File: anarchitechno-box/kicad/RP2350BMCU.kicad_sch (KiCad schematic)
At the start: 51 parts, among them J1 C2988369, J10 Conn_01x04, J2 Conn_01x03_Socket, J8 Conn_01x04, Q1 12mhz, SW1 C318884, SW2 RotaryEncoder_Switch_MP, U4 <value>, U6 TLV74311PDBVR, U7 C85364

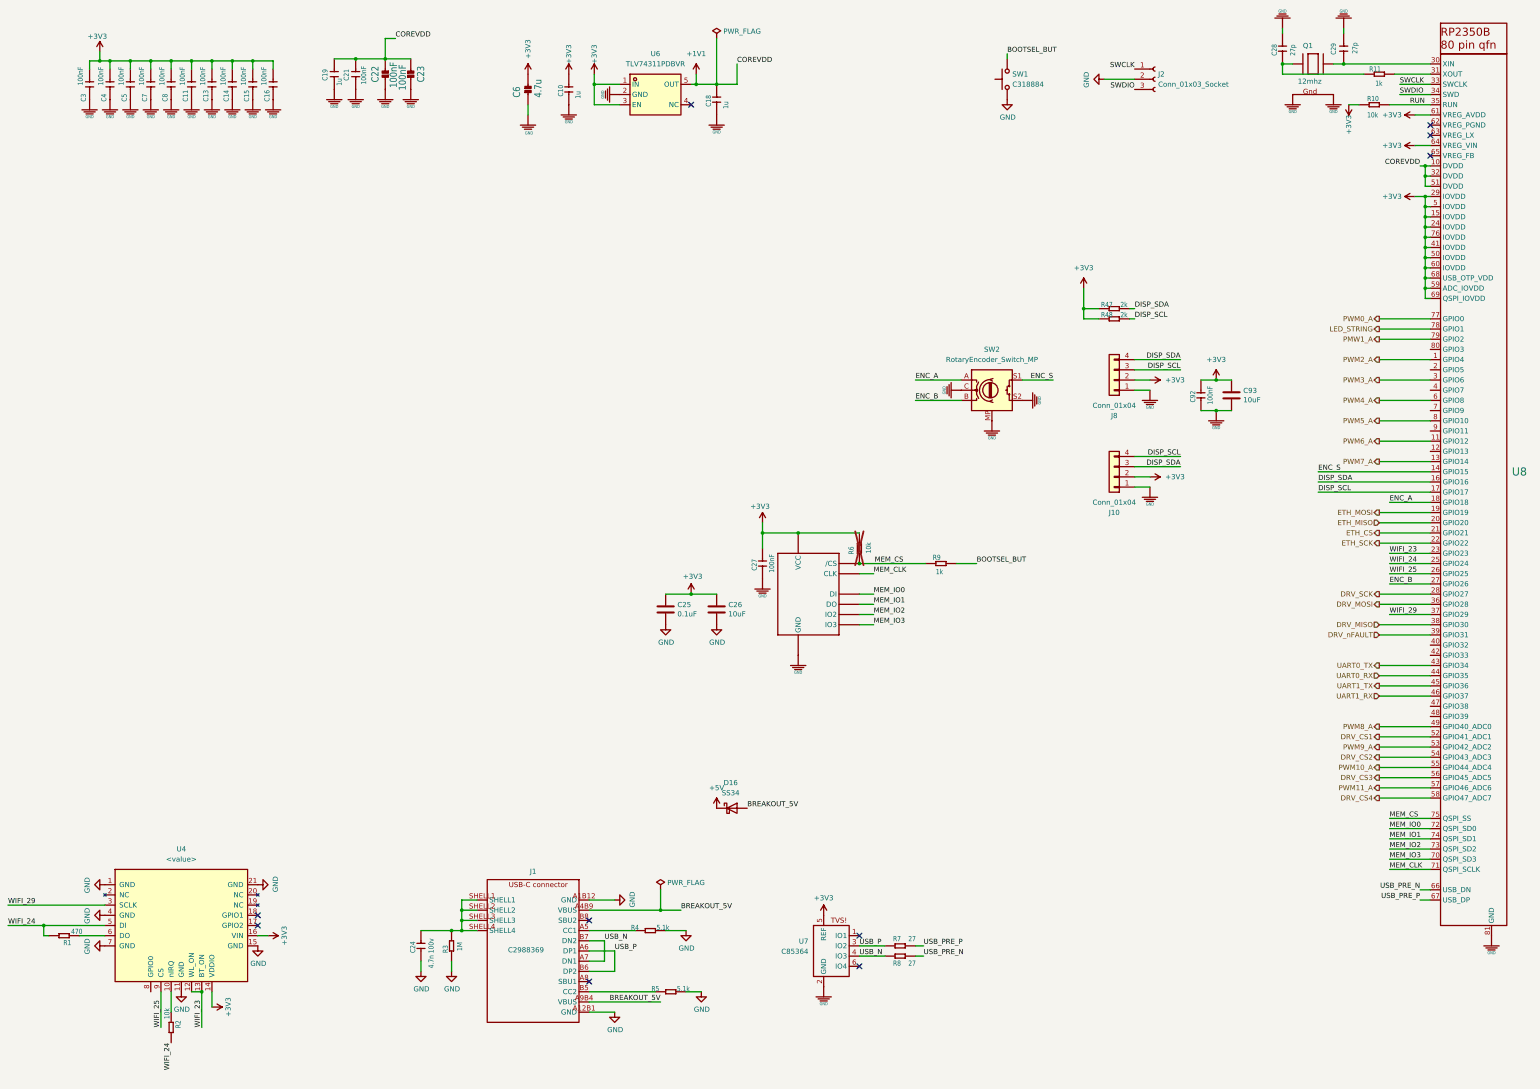
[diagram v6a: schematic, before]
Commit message: Schematic & PCB changes: - Cleaned up unnecessary electrolytic input capacitor flyback - Removed dual diode rectification on 5V, increased output capacitors - Feedback resistors DC/DCs set, enlarged for JLC basic parts - Sweep through schematic to consolidate caps to JLC basic parts (see list schematic front page) - Midi OUTPUT added (please check schematic) - Wiznet W5500 schematic reworked to RJ45 reference schematic: https://docs.wiznet.io/assets/files/w5500_sch_v110_use_mag_-dfff8bbb103d13be4f25cd2b2f8b950d.pdf - Replaced ethernet jack to HR911105A - Crystals chosen for W5500 and RP2350B (according to reference), 15pF load caps. - RS485 driver changed to SP3485EN for 3.3V operation - Replaced RS485 bus connectors with 2x RJ45s for passthrough - Groove connector replaced with JST XH 2mm - Added LCSC part numbers for various components in the schematic
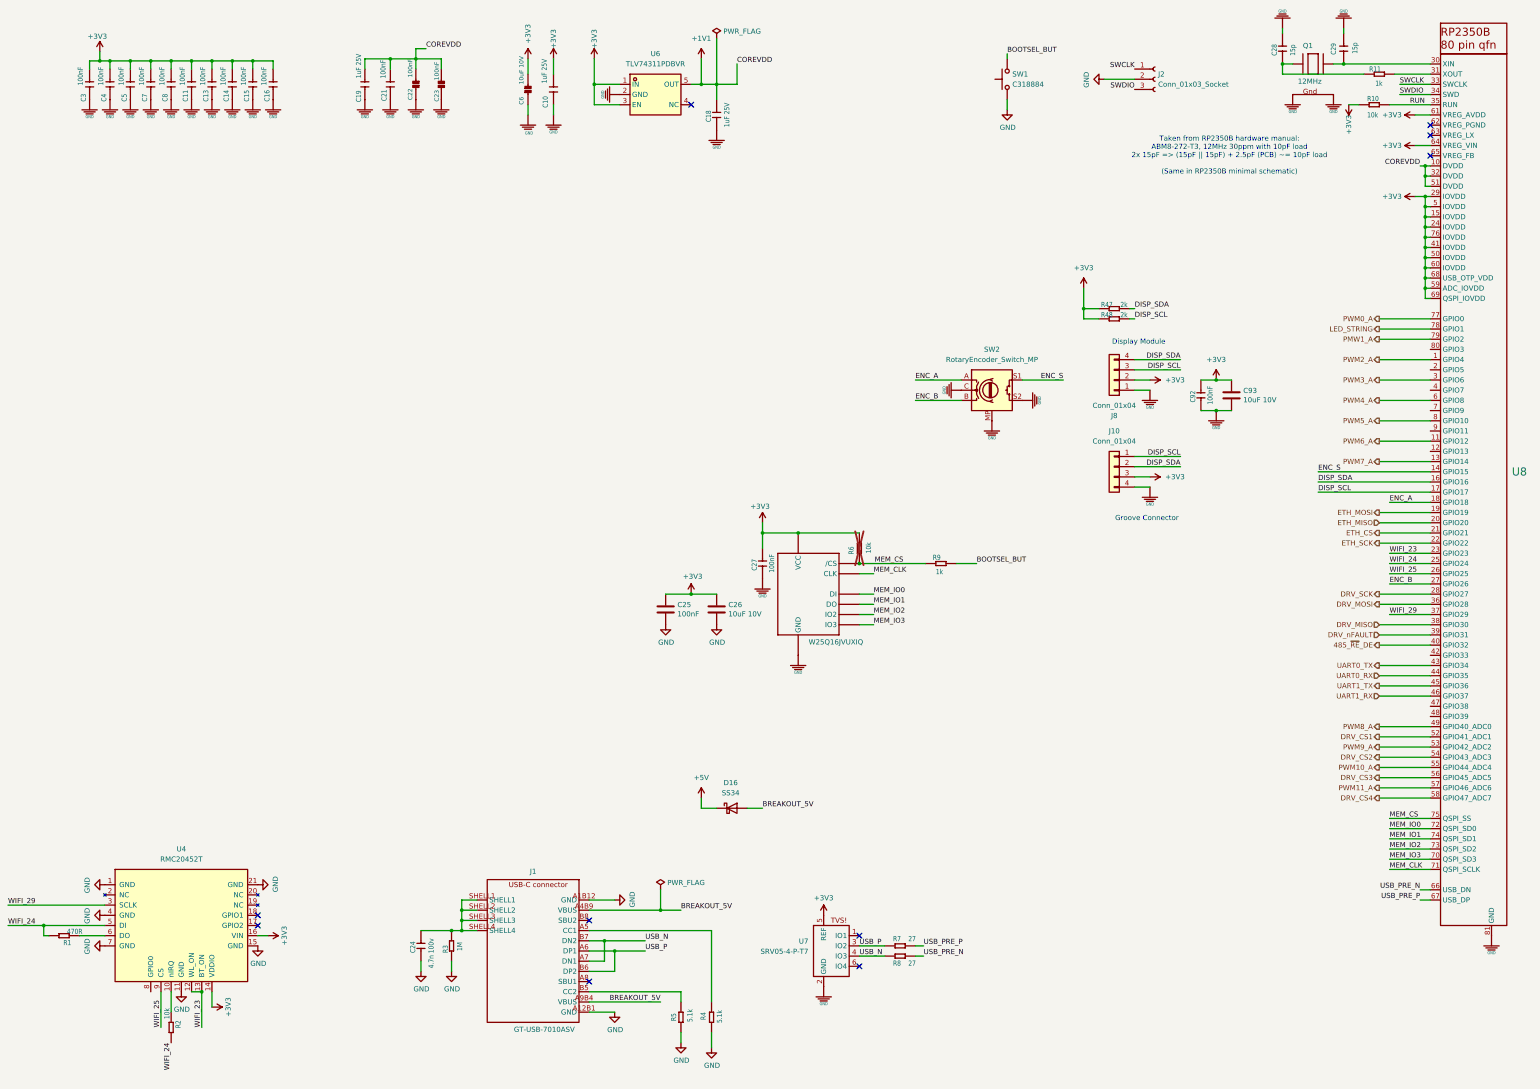
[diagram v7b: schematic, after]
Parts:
- C10, C18: value 1u -> 1uF 25V; LCSC Part (none) -> C52923
- C19: value 1u -> 1uF 25V; LSCS Part (none) -> C52923
- C24: LCSC Part (none) -> C577156
- C25: value 0.1uF -> 100nF; Digi-Key_PN 311-1344-1-ND -> (none)
- C26, C93: value 10uF -> 10uF 10V; Digi-Key_PN 311-1344-1-ND -> (none); LCSC Part (none) -> C19702
- C28, C29: value 27p -> 15p; LCSC Part (none) -> C1548
- C6: value 4.7u -> 10uF 10V; footprint Capacitor_SMD:C_0402_1005Metric -> Capacitor_SMD:C_0603_1608Metric; LCSC Part (none) -> C19702
- J1: value C2988369 -> GT-USB-7010ASV; LCSC Part (none) -> C2988369
- J10: footprint Connector_PinHeader_2.54mm:PinHeader_1x04_P2.54mm_Vertical -> Connectors:Grove_1x04
- Q1: value 12mhz -> 12MHz; LCSC Part (none) -> C20625731
- R1: value 470 -> 470R; footprint Resistor_SMD:R_0603_1608Metric -> Resistor_SMD:R_0402_1005Metric
- R2: footprint Resistor_SMD:R_0603_1608Metric -> Resistor_SMD:R_0402_1005Metric
- R3: LCSC Part (none) -> C22935
- R4, R5: LCSC Part (none) -> C23186
- SW1: LCSC Part (none) -> C318884
- U$1: value C2843335 W25Q16JVUXIQ -> W25Q16JVUXIQ; LCSC Part (none) -> C2843335
- U4: value <value> -> RMC20452T; LCSC Part (none) -> C49451547
- U7: value C85364 -> SRV05-4-P-T7; LCSC Part (none) -> C85364
- U8: LCSC Part (none) -> C42415655
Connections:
- net +3V3: now also J10.3 (Pin_3); no longer J10.2 (Pin_2)
- net DISP_SCL: now also J10.1 (Pin_1); no longer J10.4 (Pin_4)
- net DISP_SDA: now also J10.2 (Pin_2); no longer J10.3 (Pin_3)
- net GND: now also J10.4 (Pin_4); no longer J10.1 (Pin_1)
- net 485_~{RE}_DE: now reaches U8.40 (GPIO32)
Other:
- note added: "Display Module"
- note added: "Groove Connector"
- note added: "Taken from RP2350B hardware manual: ABM8-272-T3, 12MHz 30ppm with 10pF load 2x 15pF => (15pF || 15pF) + 2.5pF (PCB) ~= 10pF load (Same in RP2350B minimal schematic)"
- moved on the sheet: C10, C18, C19, C21, C22, C23, J10, R4, R5

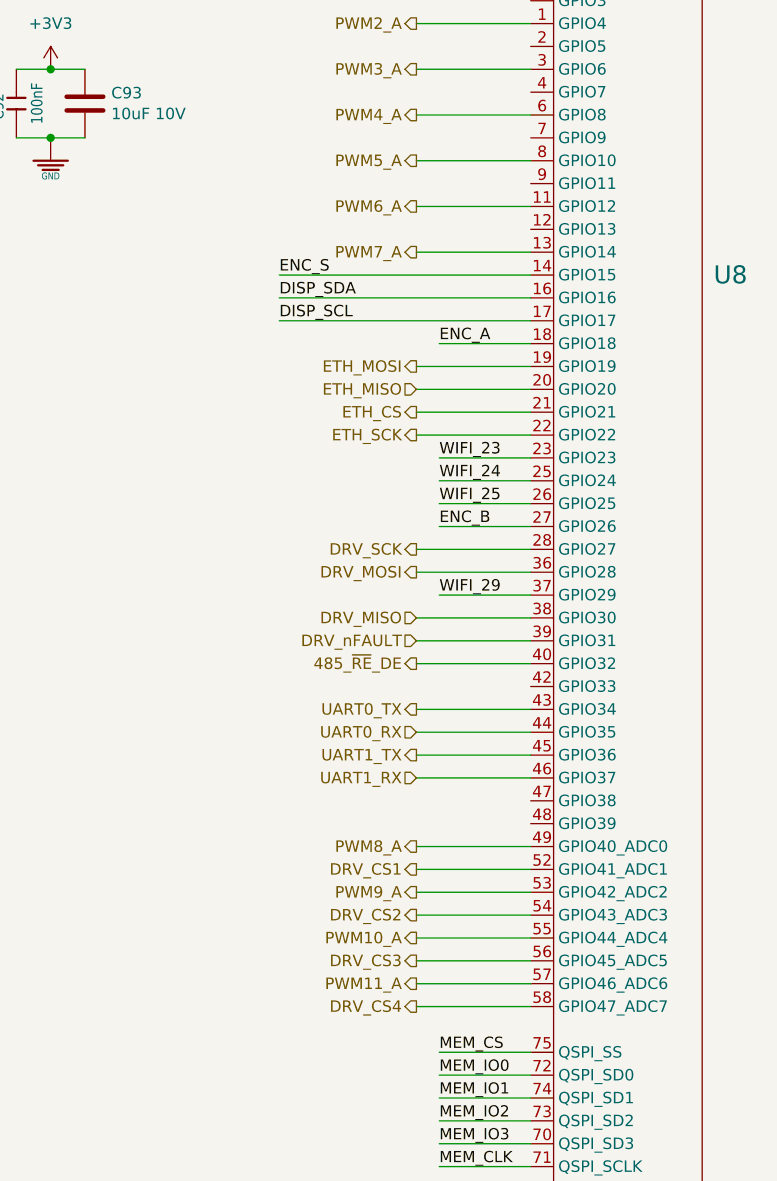
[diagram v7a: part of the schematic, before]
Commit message: - Thermische berekening DRV8245 vs losse transistors - DRV8245 package gecorrigeerd naar TSSOP-28 - Layout aangepast om grotere package te passen - 1x GND output per kanaal - Waarschijnlijk geen 140mm fan nodig => print weer gekropmen - RS485 power line gefixed (3.3V vs 3V3P) - Kleine BOM en I/O wijzigingen tbv layout
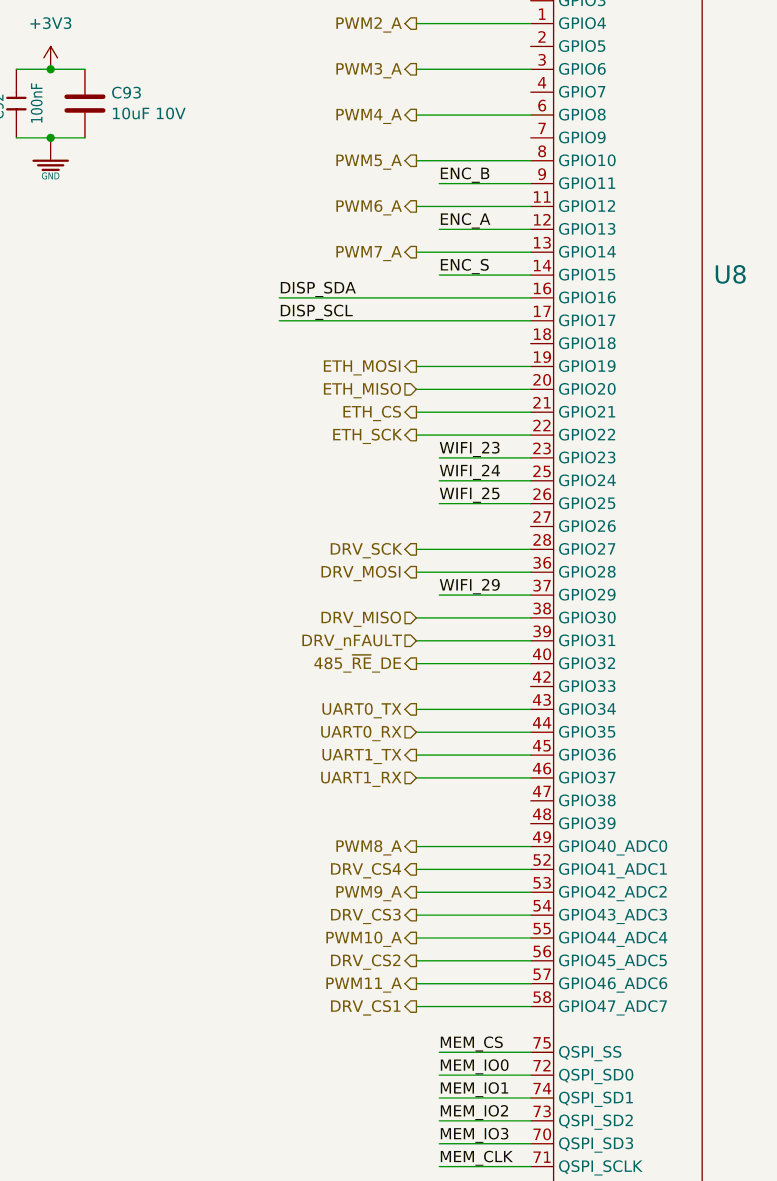
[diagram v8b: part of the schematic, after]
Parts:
- R7, R8: footprint Resistor_SMD:R_0603_1608Metric -> Resistor_SMD:R_0402_1005Metric; LCSC Part (none) -> C138021
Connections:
- net DRV_CS1: now also U8.58 (GPIO47_ADC7); no longer U8.52 (GPIO41_ADC1)
- net DRV_CS2: now also U8.56 (GPIO45_ADC5); no longer U8.54 (GPIO43_ADC3)
- net DRV_CS3: now also U8.54 (GPIO43_ADC3); no longer U8.56 (GPIO45_ADC5)
- net DRV_CS4: now also U8.52 (GPIO41_ADC1); no longer U8.58 (GPIO47_ADC7)
- net ENC_A: now also U8.12 (GPIO13); no longer U8.18 (GPIO18)
- net ENC_B: now also U8.9 (GPIO11); no longer U8.27 (GPIO26)
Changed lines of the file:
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@@
 	(wire
 		(pts
-			(xy 351.79 130.81) (xy 379.73 130.81)
-		)
-		(stroke
-			(width 0)
-			(type default)
-		)
-	)
-	(wire
-		(pts
 			(xy 243.84 248.92) (xy 237.49 248.92)
 		)
@@
 	(wire
 		(pts
+			(xy 367.03 207.01) (xy 379.73 207.01)
+		)
+		(stroke
+			(width 0)
+			(type default)
+		)
+	)
+	(wire
+		(pts
 			(xy 317.5 105.41) (xy 306.07 105.41)
 		)
@@
 	(wire
 		(pts
+			(xy 367.03 201.93) (xy 379.73 201.93)
+		)
+		(stroke
+			(width 0)
+			(type default)
+		)
+	)
+	(wire
+		(pts
 			(xy 361.95 39.37) (xy 359.41 39.37)
 		)
@@
 	(wire
 		(pts
-			(xy 367.03 196.85) (xy 379.73 196.85)
+			(xy 237.49 166.37) (xy 241.046 166.37)
 		)
 		(stroke
@@
 	(wire
 		(pts
-			(xy 237.49 166.37) (xy 241.046 166.37)
+			(xy 377.19 234.95) (xy 379.73 234.95)
 		)
 		(stroke
@@
 	(wire
 		(pts
-			(xy 377.19 234.95) (xy 379.73 234.95)
+			(xy 367.03 196.85) (xy 379.73 196.85)
 		)
 		(stroke
@@
 	(wire
 		(pts
-			(xy 369.57 158.75) (xy 379.73 158.75)
-		)
-		(stroke
-			(width 0)
-			(type default)
-		)
-	)
-	(wire
-		(pts
 			(xy 48.26 26.162) (xy 48.26 28.448)
 		)
@@
 	(wire
 		(pts
+			(xy 367.03 212.09) (xy 379.73 212.09)
+		)
+		(stroke
+			(width 0)
+			(type default)
+		)
+	)
+	(wire
+		(pts
 			(xy 378.46 54.61) (xy 379.73 54.61)
 		)
@@
 	(wire
 		(pts
+			(xy 369.57 125.73) (xy 379.73 125.73)
+		)
+		(stroke
+			(width 0)
+			(type default)
+		)
+	)
+	(wire
+		(pts
 			(xy 198.12 214.63) (xy 201.93 214.63)
 		)
@@
 	(wire
 		(pts
-			(xy 369.57 138.43) (xy 379.73 138.43)
+			(xy 317.5 129.54) (xy 306.07 129.54)
 		)
 		(stroke
@@
 	(wire
 		(pts
-			(xy 317.5 129.54) (xy 306.07 129.54)
+			(xy 309.88 132.08) (xy 306.07 132.08)
 		)
 		(stroke
@@
 	(wire
 		(pts
-			(xy 309.88 132.08) (xy 306.07 132.08)
+			(xy 370.84 31.75) (xy 379.73 31.75)
 		)
 		(stroke
@@
 	(wire
 		(pts
-			(xy 370.84 31.75) (xy 379.73 31.75)
+			(xy 25.4 238.76) (xy 49.53 238.76)
 		)
 		(stroke
@@
 	(wire
 		(pts
-			(xy 25.4 238.76) (xy 49.53 238.76)
+			(xy 369.57 120.65) (xy 379.73 120.65)
 		)
 		(stroke
@@
 	(wire
 		(pts
+			(xy 369.57 130.81) (xy 379.73 130.81)
+		)
+		(stroke
+			(width 0)
+			(type default)
+		)
+	)
+	(wire
+		(pts
 			(xy 367.03 123.19) (xy 379.73 123.19)
 		)
@@
 	(wire
 		(pts
-			(xy 367.03 212.09) (xy 379.73 212.09)
-		)
-		(stroke
-			(width 0)
-			(type default)
-		)
-	)
-	(wire
-		(pts
 			(xy 304.8 90.17) (xy 306.07 90.17)
 		)
@@
 	(wire
 		(pts
-			(xy 367.03 201.93) (xy 379.73 201.93)
-		)
-		(stroke
-			(width 0)
-			(type default)
-		)
-	)
-	(wire
-		(pts
 			(xy 293.37 85.09) (xy 293.37 90.17)
 		)
@@
 	(wire
 		(pts
-			(xy 367.03 207.01) (xy 379.73 207.01)
-		)
-		(stroke
-			(width 0)
-			(type default)
-		)
-	)
-	(wire
-		(pts
 			(xy 367.03 179.07) (xy 379.73 179.07)
 		)
@@
 	)
 	(label "ENC_S"
+		(at 369.57 130.81 0)
+		(effects
+			(font
+				(size 1.27 1.27)
+			)
+			(justify left bottom)
+		)
+	)
+	(label "ENC_S"
 		(at 288.29 107.95 180)
 		(effects
@@
 		)
 	)
-	(label "ENC_A"
-		(at 369.57 138.43 0)
-		(effects
-			(font
-				(size 1.27 1.27)
-			)
-			(justify left bottom)
-		)
-	)
 	(label "WIFI_23"
 		(at 73.66 269.24 90)
@@
 	)
 	(label "ENC_B"
-		(at 369.57 158.75 0)
+		(at 369.57 120.65 0)
+		(effects
+			(font
+				(size 1.27 1.27)
+			)
+			(justify left bottom)
+		)
+	)
+	(label "ENC_A"
+		(at 369.57 125.73 0)
 		(effects
 			(font
@@
 		)
 	)
-	(label "ENC_S"
-		(at 351.79 130.81 0)
-		(effects
-			(font
-				(size 1.27 1.27)
-			)
-			(justify left bottom)
-		)
-	)
 	(label "DISP_SDA"
 		(at 317.5 129.54 180)
@@
 		)
 	)
-	(hierarchical_label "DRV_CS4"
-		(shape output)
-		(at 367.03 212.09 180)
-		(effects
-			(font
-				(size 1.27 1.27)
-			)
-			(justify right)
-		)
-	)
-	(hierarchical_label "DRV_CS3"
-		(shape output)
-		(at 367.03 207.01 180)
-		(effects
-			(font
-				(size 1.27 1.27)
-			)
-			(justify right)
-		)
-	)
 	(hierarchical_label "PWM11_A"
 		(shape output)
@@
 		)
 	)
+	(hierarchical_label "DRV_CS2"
+		(shape output)
+		(at 367.03 207.01 180)
+		(effects
+			(font
+				(size 1.27 1.27)
+			)
+			(justify right)
+		)
+	)
 	(hierarchical_label "PWM4_A"
 		(shape output)
@@
 		)
 	)
-	(hierarchical_label "DRV_CS2"
-		(shape output)
-		(at 367.03 201.93 180)
-		(effects
-			(font
-				(size 1.27 1.27)
-			)
-			(justify right)
-		)
-	)
 	(hierarchical_label "PWM9_A"
 		(shape output)
@@
 		)
 	)
-	(hierarchical_label "DRV_CS1"
-		(shape output)
-		(at 367.03 196.85 180)
+	(hierarchical_label "DRV_nFAULT"
+		(shape input)
+		(at 367.03 171.45 180)
 		(effects
 			(font
@@
 		)
 	)
-	(hierarchical_label "DRV_nFAULT"
-		(shape input)
-		(at 367.03 171.45 180)
+	(hierarchical_label "DRV_CS1"
+		(shape output)
+		(at 367.03 212.09 180)
 		(effects
 			(font
@@
 		)
 	)
+	(hierarchical_label "DRV_CS4"
+		(shape output)
+		(at 367.03 196.85 180)
+		(effects
+			(font
+				(size 1.27 1.27)
+			)
+			(justify right)
+		)
+	)
 	(hierarchical_label "UART1_TX"
 		(shape output)
@@
 		)
 	)
+	(hierarchical_label "DRV_CS3"
+		(shape output)
+		(at 367.03 201.93 180)
+		(effects
+			(font
+				(size 1.27 1.27)
+			)
+			(justify right)
+		)
+	)
 	(hierarchical_label "PWM7_A"
 		(shape output)
@@
 			)
 		)
-		(property "Footprint" "Resistor_SMD:R_0603_1608Metric"
+		(property "Footprint" "Resistor_SMD:R_0402_1005Metric"
 			(at 247.65 251.46 0)
 			(effects
@@
 			)
 		)
+		(property "LCSC Part" "C138021"
+			(at 247.65 251.46 0)
+			(effects
+				(font
+					(size 1.27 1.27)
+				)
+				(hide yes)
+			)
+		)
 		(pin "1"
 		)
@@
 			)
 		)
-		(property "Footprint" "Resistor_SMD:R_0603_1608Metric"
+		(property "Footprint" "Resistor_SMD:R_0402_1005Metric"
 			(at 247.65 248.92 0)
 			(effects
@@
 			(at 247.65 248.92 0)
 			(effects
+				(font
+					(size 1.27 1.27)
+				)
+				(hide yes)
+			)
+		)
+		(property "LCSC Part" "C138021"
+			(at 247.65 248.92 0)
+			(effects
